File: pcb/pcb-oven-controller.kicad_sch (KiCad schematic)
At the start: 17 parts, among them J1 USB_A, SW1 SW_Push, U1 STM32F411CEUx, Y1 25Mhz

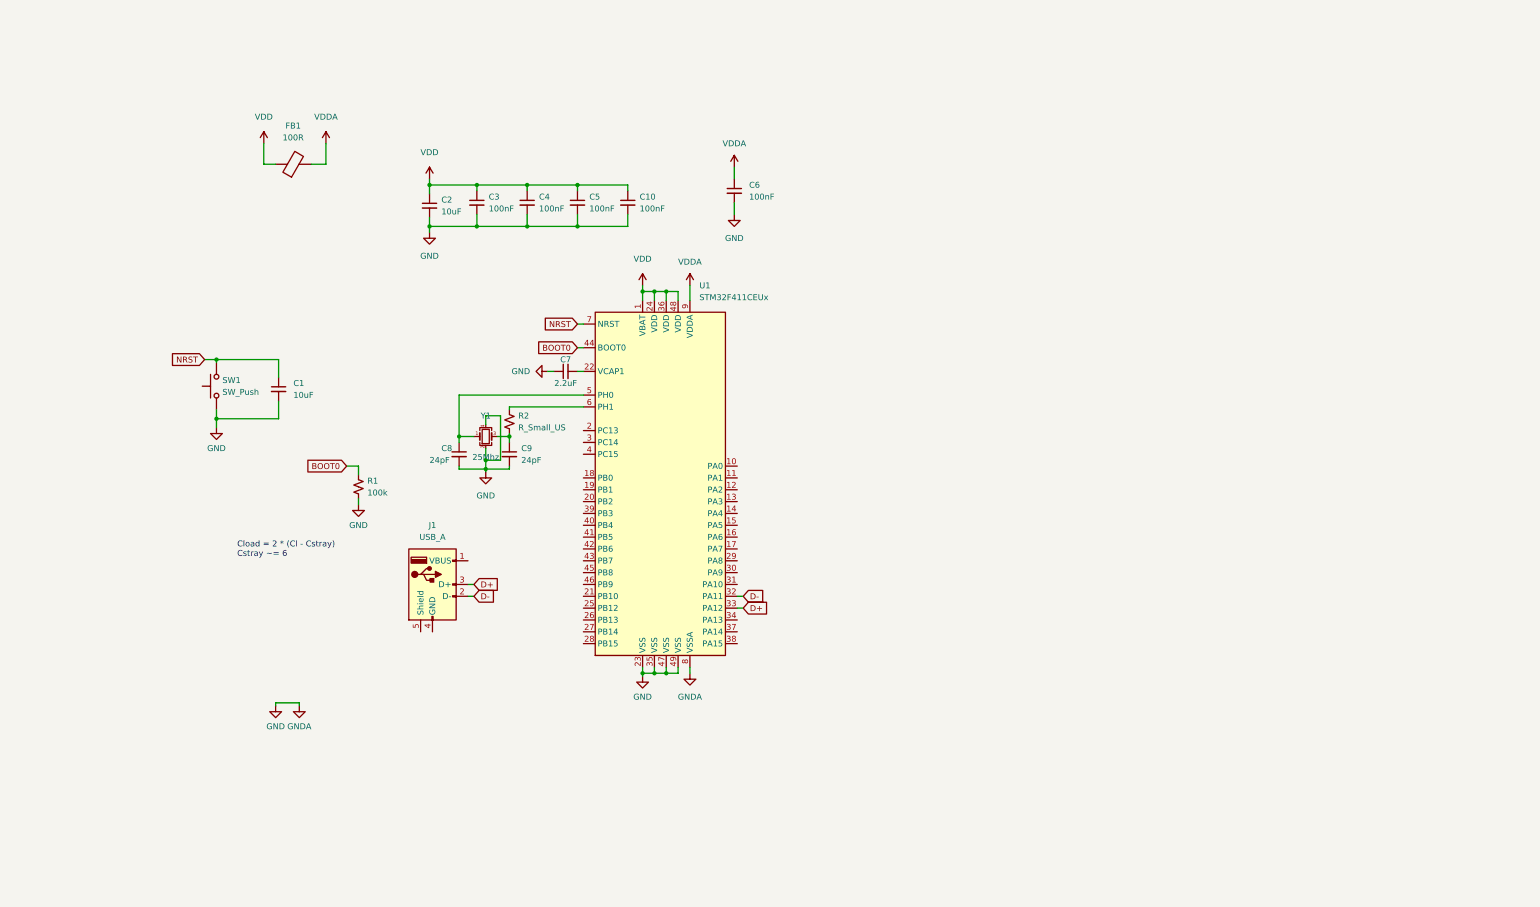
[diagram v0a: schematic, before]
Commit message: Add MicroSD, digital I/O expander, and initial thermocouple IC
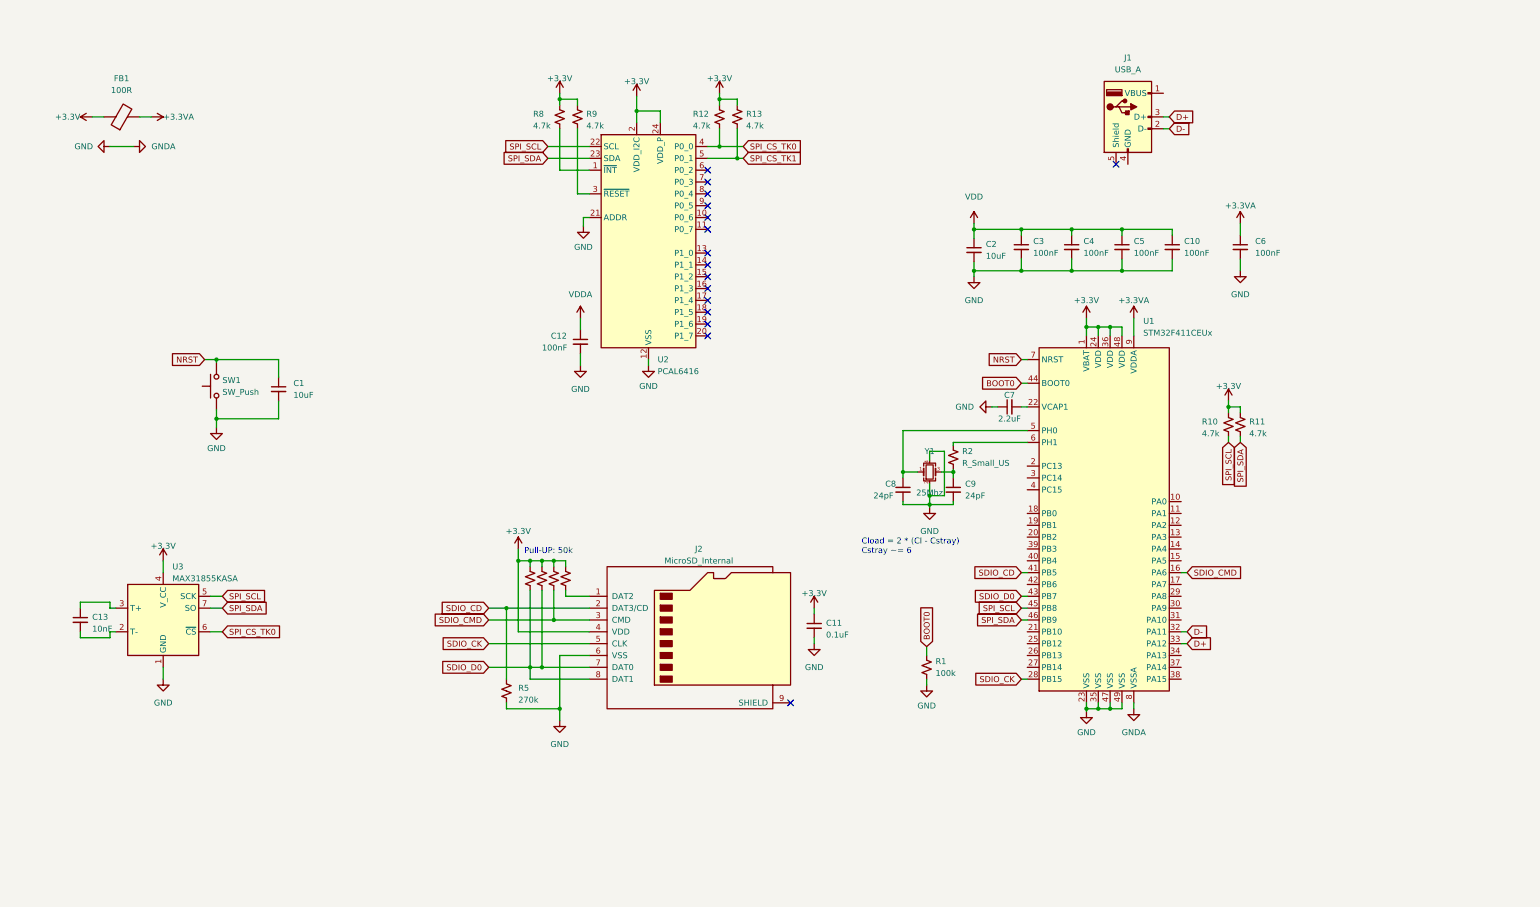
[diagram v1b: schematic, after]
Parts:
- added C11: 0.1uF, symbol Device:C_Small
- added C12: 100nF, Capacitor_SMD:C_0402_1005Metric, symbol Device:C_Small
- added C13: 10nF, symbol Device:C_Small
- added J2: MicroSD_Internal, symbol Connector:Micro_SD_Card
- added R10, R11, R12, R13, R8, R9: 4.7k, symbol Device:R_Small_US
- added R3, R4, R6, R7: 50k, symbol Device:R_Small_US
- added R5: 270k, symbol Device:R_Small_US
- added U2: PCAL6416, Package_DFN_QFN:WQFN-24-1EP_4x4mm_P0.5mm_EP2.45x2.45mm, symbol ATL:PCAL6416
- added U3: MAX31855KASA, Package_SO:SOIC-8_3.9x4.9mm_P1.27mm, symbol Sensor_Temperature:MAX31855KASA
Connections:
- net GND: now also C11.2, C12.2, J2.6 (VSS), R5.2, U2.12 (VSS), U2.21 (ADDR), U3.1 (GND)
- net VDD: no longer FB1.1, U1.1 (VBAT), U1.24 (VDD), U1.36 (VDD), U1.48 (VDD)
- net VDDA: now also C12.1; no longer C6.1, FB1.2, U1.9 (VDDA)
- net SDIO_CMD: now reaches U1.16 (PA6)
- net SDIO_CMD: now also J2.3 (CMD), R4.2
- net SDIO_CK: now reaches U1.28 (PB15)
- net SDIO_CK: now also J2.5 (CLK)
- net SDIO_CD: now reaches U1.41 (PB5)
- net SDIO_CD: now also J2.2 (DAT3/CD), R5.1
- net SDIO_D0: now reaches U1.43 (PB7)
- net SDIO_D0: now also J2.7 (DAT0), J2.8 (DAT1), R6.2, R7.2
- net SPI_SCL: now reaches U1.45 (PB8)
- net SPI_SCL: now also R10.2, U2.22 (SCL), U3.5 (SCK)
- net SPI_SDA: now reaches U1.46 (PB9)
- net SPI_SDA: now also R11.2, U2.23 (SDA), U3.7 (SO)
- new net: C13.2, U3.2 (T-)
- new net: C13.1, U3.3 (T+)
- new net: R8.2, U2.1 (~{INT})
- new net: J2.1 (DAT2), R3.2
- new net: R9.2, U2.3 (~{RESET})
- new net +3.3V: C11.1, FB1.1, J2.4 (VDD), R10.1, R11.1, R12.1, R13.1, R3.1, R4.1, R6.1, R7.1, R8.1, R9.1, U1.1 (VBAT), U1.24 (VDD), U1.36 (VDD), U1.48 (VDD), U2.2 (VDD_I2C), U2.24 (VDD_P), U3.4 (V_CC)
- new net +3.3VA: C6.1, FB1.2, U1.9 (VDDA)
- new net SPI_CS_TK0: R12.2, U2.4 (P0_0), U3.6 (~{CS})
- new net SPI_CS_TK1: R13.2, U2.5 (P0_1)
- no-connect marks 0 -> 16
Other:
- note added: "Pull-UP: 50k"
- moved on the sheet: C10, C2, C3, C4, C5, C6, C7, C8, C9, FB1, J1, R1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

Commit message: Add more pcb progress
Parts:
- removed C12: 100nF, Capacitor_SMD:C_0402_1005Metric, symbol Device:C_Small
- removed FB1: 100R, Inductor_SMD:L_0603_1608Metric, symbol Device:FerriteBead
- added C14, C15, C16: 10nF, Capacitor_SMD:C_0603_1608Metric, symbol Device:C_Small
- added C17: 10uF, Capacitor_SMD:C_0603_1608Metric, symbol Device:C_Small
- added C18: 100nF, Capacitor_SMD:C_0402_1005Metric, symbol Device:C_Small
- added C19, C20: 100nF, Capacitor_SMD:C_0603_1608Metric, symbol Device:C_Small
- added J3: TC2030, Connector:Tag-Connect_TC2030-IDC-NL_2x03_P1.27mm_Vertical, symbol ATL:TC2030
- added R14, R15: 4.7k, Resistor_SMD:R_0603_1608Metric, symbol Device:R_Small_US
- added TC1: Thermocouple_0, ATL:K_Thermocouple_Generic, symbol Device:Thermocouple_Block
- added TC2: Thermocouple_1, ATL:K_Thermocouple_Generic, symbol Device:Thermocouple_Block
- added U4: MAX31855KASA, Package_SO:SOIC-8_3.9x4.9mm_P1.27mm, symbol Sensor_Temperature:MAX31855KASA
- added U5, U6: TMP1075DSG, Package_SON:WSON-8-1EP_2x2mm_P0.5mm_EP0.9x1.6mm_ThermalVias, symbol Sensor_Temperature:TMP1075DSG
- C11: value 0.1uF -> 100nF; footprint (none) -> Capacitor_SMD:C_0603_1608Metric
- C13: footprint (none) -> Capacitor_SMD:C_0603_1608Metric
- R10, R3, R4, R5, R6, R7, R8, R9: footprint (none) -> Resistor_SMD:R_0603_1608Metric
- R11, R12, R13: footprint (none) -> Resistor_SMD:R_0603_1608Metric_Pad0.98x0.95mm_HandSolder
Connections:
- net +3.3V: now also C15.1, C16.1, C19.1, C20.1, R14.2, R15.2, U4.4 (V_CC), U5.8 (V+), U6.7 (A0), U6.8 (V+)
- net GND: now also J1.4 (GND), C15.2, C16.2, C17.2, C18.2, C19.2, C20.2, J3.5 (GND), U4.1 (GND), U5.4 (GND), U5.5 (A2), U5.6 (A1), U5.7 (A0), U5.9 (EP), U6.4 (GND), U6.5 (A2), U6.6 (A1), U6.9 (EP); no longer U1.8 (VSSA)
- net NRST: now also J3.3 (~{RESET})
- net SPI_CS_TK1: now also U4.6 (~{CS})
- net SPI_SCL: now also U4.5 (SCK); no longer R10.2, U1.45 (PB8), U2.22 (SCL)
- net SPI_SDA: now also U4.7 (SO); no longer R11.2, U1.46 (PB9), U2.23 (SDA)
- net VDD: now also C17.1, C18.1
- net at C13.2, U3.2 (T-): now also TC1.2 (-)
- net at C13.1, U3.3 (T+): now also TC1.1 (+)
- net SWDIO: now reaches U1.34 (PA13)
- net SWDIO: now also J3.2 (SWDIO)
- net SWCLK: now reaches U1.37 (PA14)
- net SWCLK: now also J3.4 (SWCLK)
- net SWO: now reaches U1.39 (PB3)
- net SWO: now also J3.6 (SWO)
- new net: R14.1, U5.3 (ALERT)
- new net: R15.1, U6.3 (ALERT)
- new net: C14.2, TC2.2 (-), U4.2 (T-)
- new net: C14.1, TC2.1 (+), U4.3 (T+)
- new net GNDA: U1.8 (VSSA)
- new net I2C_SCL: R10.2, U1.45 (PB8), U2.22 (SCL), U5.2 (SCL), U6.2 (SCL)
- new net I2C_SDA: R11.2, U1.46 (PB9), U2.23 (SDA), U5.1 (SDA), U6.1 (SDA)
- no-connect marks 16 -> 18
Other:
- added sheet Power (untitled.kicad_sch)
- note added: "Reset Button"
- note added: "SPI Chip Select"
- note added: "Temperature Monitoring"
- note added: "Thermocouple"
- moved on the sheet: C1, C11, C13, J1, J2, R10, R11, R12, R13, R5, R8, R9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
